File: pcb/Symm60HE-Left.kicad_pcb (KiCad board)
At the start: 2 copper layers, 158.9 x 107.8 mm, 115 parts

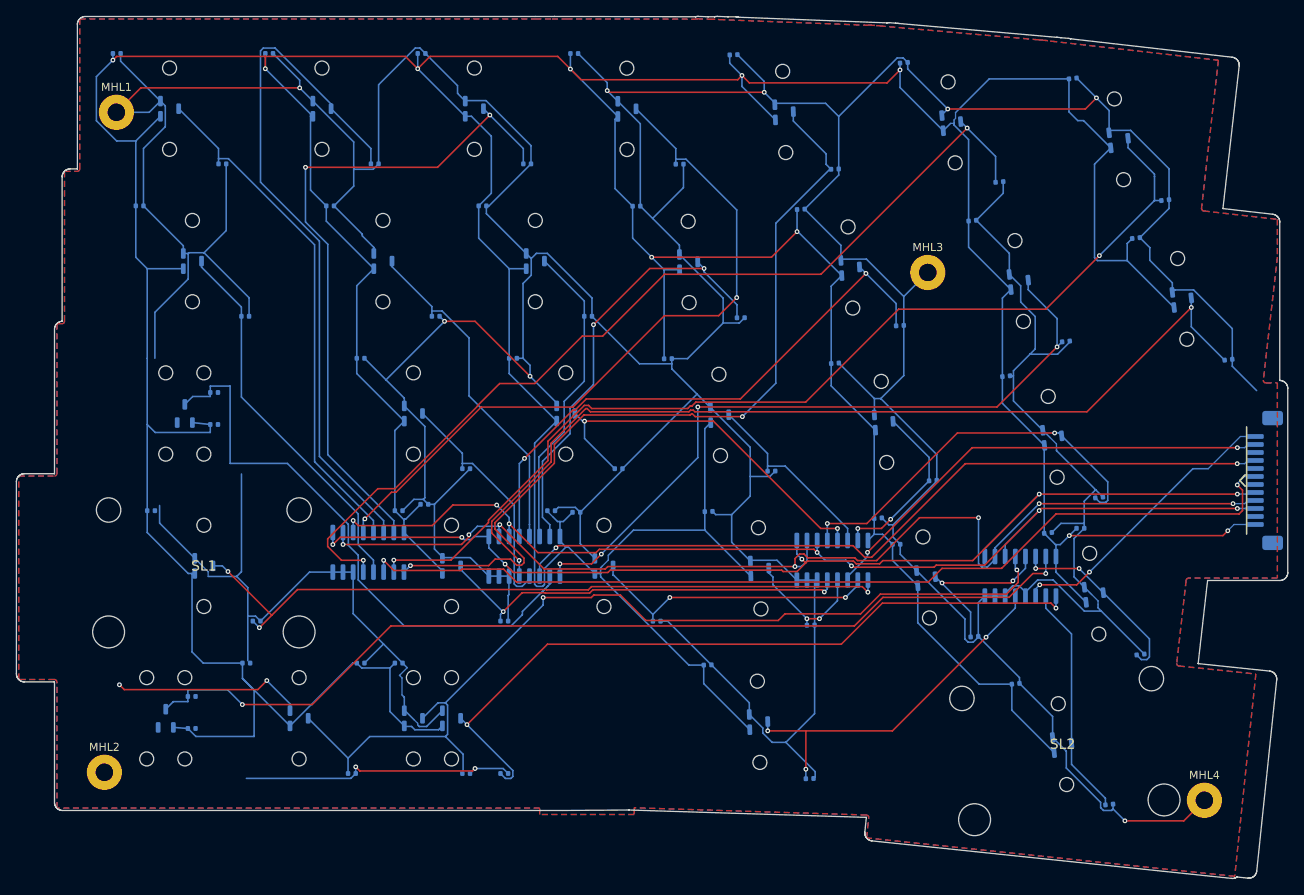
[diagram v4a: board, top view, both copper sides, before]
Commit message: Replace the project with the reorganised T7 tree: ribbon keyboard is production, pogo archived
Production design is now the outward-facing FPC keyboard with per-key
SK6812MINI-E reverse-mount LEDs, a fifth SN74LV4051A mux per half so every
alternate Hall position has its own channel, an SN74AHCT1G125 LED level
shifter, a 50 x 31 mm daughterboard, 1.5 mm POM plates and 3 degree / 7 degree
tent and typing angles. The universal half panel is fully populated (359
placements) with routed NPTH alignment slots for the mutually exclusive
positions, and eight fixed-layout Left/Right PCB pairs are released under
release/layout-pcbs/ with matching BOM, CPL, Gerber ZIP, drill report and DRC.

Reorganise tools/ into cad/, generators/, layouts/, pcb/, pogo/, releases/ and
rendering/ subpackages; add designs/ and layout/ (KLE) trees and per-layout
gallery renders. The Fusion handoff is a fourteen-body reference STEP with
Gateron KS-20 switch and Cherry-profile keycap references and exact BOOMELE,
HRO and XKB models under case/fusion360/models/official/ with provenance.

The Neo-style pogo variant, its Mill-Max vendor models, the Fusion setup
script and the pogo release packages are archived as design history and
marked DO-NOT-ORDER. Their restored BOM snapshots had reintroduced the wrong
mux part C7792; corrected to C128414 / SN74LV4051ADR and their checksum lists
and archives rebuilt.

Co-Authored-By: Claude Opus 5 <noreply@anthropic.com>
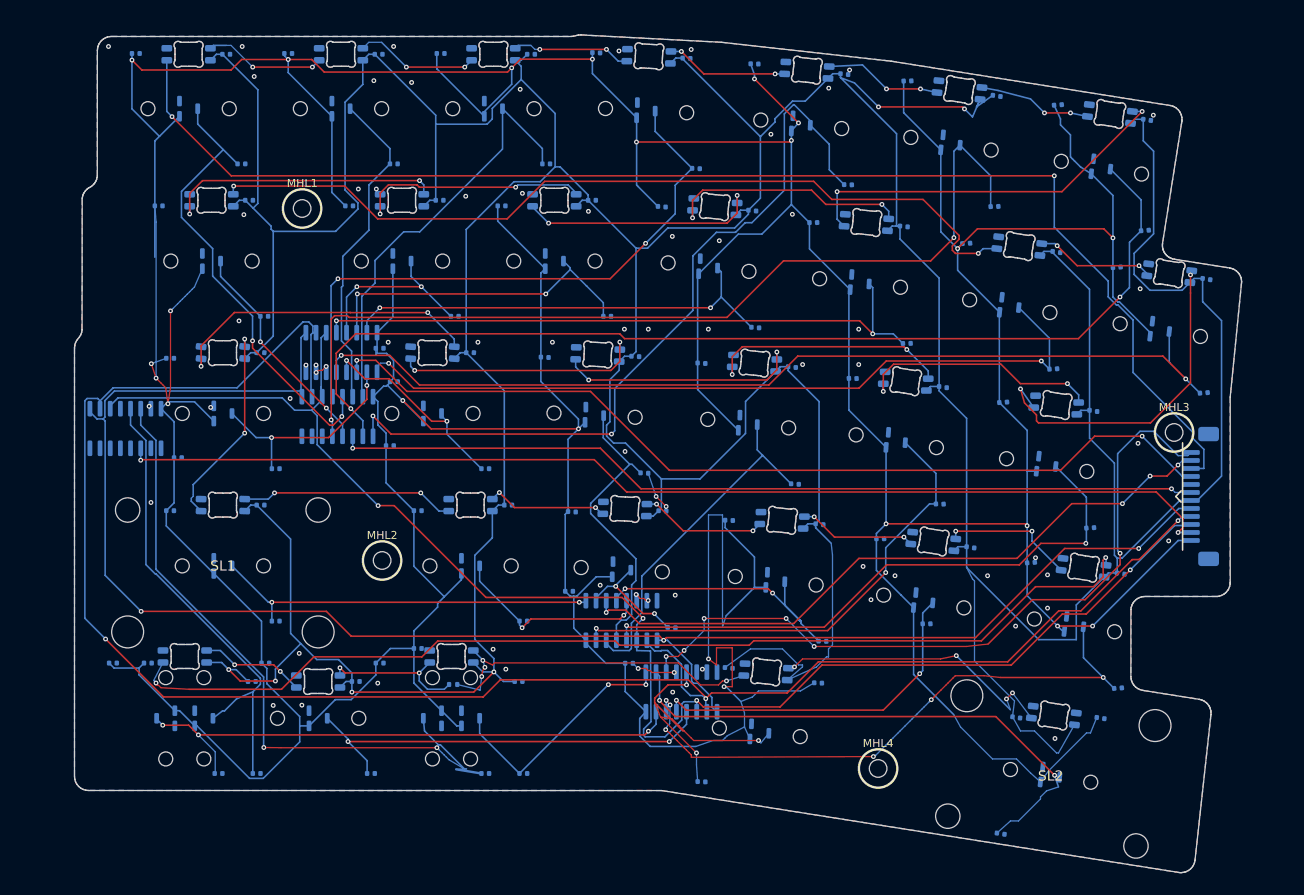
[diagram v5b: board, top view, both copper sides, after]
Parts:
- removed KML15N, KML15S, KML27A, KML27N: MX_MECHANICAL_ONLY, HE_KEY_MECHANICAL_ONLY
- added AML5: SN74LV4051A, Symm60HE_Project:AM1_SOIC-16_3.9x9.9mm_P1.27mm, B.Cu at (5.92, 49.5)
- added CL28A: 100n, Symm60HE_Project:C1_C_0402_1005Metric, B.Cu at (8.71, 78.8)
- added CL28B: 4.7n, Symm60HE_Project:C1_C_0402_1005Metric, B.Cu at (22.3, 92.6)
- added CML5: 100n, Symm60HE_Project:C1_C_0402_1005Metric, B.Cu at (12.5, 53.1)
- added CRGBL1: 100n, Symm60HE_Project:C1_C_0402_1005Metric, B.Cu at (18.5, 2.73)
- added CRGBL10: 100n, Symm60HE_Project:C1_C_0402_1005Metric, B.Cu at (64.2, 21.0)
- added CRGBL11: 100n, Symm60HE_Project:C1_C_0402_1005Metric, B.Cu at (45.2, 21.0)
- added CRGBL12: 100n, Symm60HE_Project:C1_C_0402_1005Metric, B.Cu at (21.4, 21.0)
- added CRGBL13: 100n, Symm60HE_Project:C1_C_0402_1005Metric, B.Cu at (122.3, 27.4)
- added CRGBL14: 100n, Symm60HE_Project:C1_C_0402_1005Metric, B.Cu at (141.0, 30.8)
- added CRGBL15: 100n, Symm60HE_Project:C1_C_0402_1005Metric, B.Cu at (126.9, 47.3)
- added CRGBL16: 100n, Symm60HE_Project:C1_C_0402_1005Metric, B.Cu at (108.1, 44.3)
- added CRGBL17: 100n, Symm60HE_Project:C1_C_0402_1005Metric, B.Cu at (89.2, 41.8)
- added CRGBL18: 100n, Symm60HE_Project:C1_C_0402_1005Metric, B.Cu at (69.6, 40.5)
- added CRGBL19: 100n, Symm60HE_Project:C1_C_0402_1005Metric, B.Cu at (49.0, 40.0)
- added CRGBL2: 100n, Symm60HE_Project:C1_C_0402_1005Metric, B.Cu at (37.6, 2.73)
- added CRGBL20: 100n, Symm60HE_Project:C1_C_0402_1005Metric, B.Cu at (22.8, 40.0)
- added CRGBL21: 100n, Symm60HE_Project:C1_C_0402_1005Metric, B.Cu at (22.8, 59.1)
- added CRGBL22: 100n, Symm60HE_Project:C1_C_0402_1005Metric, B.Cu at (53.8, 59.1)
- added CRGBL23: 100n, Symm60HE_Project:C1_C_0402_1005Metric, B.Cu at (73.0, 59.8)
- added CRGBL24: 100n, Symm60HE_Project:C1_C_0402_1005Metric, B.Cu at (92.7, 61.5)
- added CRGBL25: 100n, Symm60HE_Project:C1_C_0402_1005Metric, B.Cu at (111.5, 64.4)
- added CRGBL26: 100n, Symm60HE_Project:C1_C_0402_1005Metric, B.Cu at (130.3, 67.6)
- added CRGBL27: 100n, Symm60HE_Project:C1_C_0402_1005Metric, B.Cu at (21.7, 81.1)
- added CRGBL29: 100n, Symm60HE_Project:C1_C_0402_1005Metric, B.Cu at (55.1, 81.1)
- added CRGBL3: 100n, Symm60HE_Project:C1_C_0402_1005Metric, B.Cu at (56.6, 2.73)
- added CRGBL30: 100n, Symm60HE_Project:C1_C_0402_1005Metric, B.Cu at (81.3, 79.4)
- added CRGBL31: 100n, Symm60HE_Project:C1_C_0402_1005Metric, B.Cu at (117.3, 85.6)
- added CRGBL33: 100n, Symm60HE_Project:C1_C_0402_1005Metric, B.Cu at (34.7, 81.1)
- added CRGBL4: 100n, Symm60HE_Project:C1_C_0402_1005Metric, B.Cu at (76.0, 3.22)
- added CRGBL5: 100n, Symm60HE_Project:C1_C_0402_1005Metric, B.Cu at (95.8, 5.21)
- added CRGBL6: 100n, Symm60HE_Project:C1_C_0402_1005Metric, B.Cu at (114.8, 7.93)
- added CRGBL7: 100n, Symm60HE_Project:C1_C_0402_1005Metric, B.Cu at (133.6, 10.9)
- added CRGBL8: 100n, Symm60HE_Project:C1_C_0402_1005Metric, B.Cu at (103.2, 24.2)
- added CRGBL9: 100n, Symm60HE_Project:C1_C_0402_1005Metric, B.Cu at (84.3, 22.3)
- added DL1: SK6812MINI-E, Symm60HE_Project:SK6812MINI-E_ReverseMount, B.Cu at (13.8, 2.73)
- added DL10: SK6812MINI-E, Symm60HE_Project:SK6812MINI-E_ReverseMount, B.Cu at (59.5, 21.0)
- added DL11: SK6812MINI-E, Symm60HE_Project:SK6812MINI-E_ReverseMount, B.Cu at (40.5, 21.0)
- added DL12: SK6812MINI-E, Symm60HE_Project:SK6812MINI-E_ReverseMount, B.Cu at (16.7, 21.0)
- added DL13: SK6812MINI-E, Symm60HE_Project:SK6812MINI-E_ReverseMount, B.Cu at (117.6, 26.7)
- added DL14: SK6812MINI-E, Symm60HE_Project:SK6812MINI-E_ReverseMount, B.Cu at (136.4, 30.1)
- added DL15: SK6812MINI-E, Symm60HE_Project:SK6812MINI-E_ReverseMount, B.Cu at (122.3, 46.6)
- added DL16: SK6812MINI-E, Symm60HE_Project:SK6812MINI-E_ReverseMount, B.Cu at (103.5, 43.6)
- added DL17: SK6812MINI-E, Symm60HE_Project:SK6812MINI-E_ReverseMount, B.Cu at (84.6, 41.3)
- added DL18: SK6812MINI-E, Symm60HE_Project:SK6812MINI-E_ReverseMount, B.Cu at (65.0, 40.2)
- added DL19: SK6812MINI-E, Symm60HE_Project:SK6812MINI-E_ReverseMount, B.Cu at (44.3, 40.0)
- added DL2: SK6812MINI-E, Symm60HE_Project:SK6812MINI-E_ReverseMount, B.Cu at (32.9, 2.73)
- added DL20: SK6812MINI-E, Symm60HE_Project:SK6812MINI-E_ReverseMount, B.Cu at (18.1, 40.0)
- added DL21: SK6812MINI-E, Symm60HE_Project:SK6812MINI-E_ReverseMount, B.Cu at (18.1, 59.1)
- added DL22: SK6812MINI-E, Symm60HE_Project:SK6812MINI-E_ReverseMount, B.Cu at (49.1, 59.1)
- added DL23: SK6812MINI-E, Symm60HE_Project:SK6812MINI-E_ReverseMount, B.Cu at (68.3, 59.6)
- added DL24: SK6812MINI-E, Symm60HE_Project:SK6812MINI-E_ReverseMount, B.Cu at (88.0, 61.0)
- added DL25: SK6812MINI-E, Symm60HE_Project:SK6812MINI-E_ReverseMount, B.Cu at (106.9, 63.6)
- added DL26: SK6812MINI-E, Symm60HE_Project:SK6812MINI-E_ReverseMount, B.Cu at (125.7, 66.9)
- added DL27: SK6812MINI-E, Symm60HE_Project:SK6812MINI-E_ReverseMount, B.Cu at (13.3, 78.0)
- added DL29: SK6812MINI-E, Symm60HE_Project:SK6812MINI-E_ReverseMount, B.Cu at (46.7, 78.0)
- added DL3: SK6812MINI-E, Symm60HE_Project:SK6812MINI-E_ReverseMount, B.Cu at (51.9, 2.73)
- added DL30: SK6812MINI-E, Symm60HE_Project:SK6812MINI-E_ReverseMount, B.Cu at (86.0, 79.9)
- added DL31: SK6812MINI-E, Symm60HE_Project:SK6812MINI-E_ReverseMount, B.Cu at (122.0, 85.4)
- added DL33: SK6812MINI-E, Symm60HE_Project:SK6812MINI-E_ReverseMount, B.Cu at (30.0, 81.1)
- added DL4: SK6812MINI-E, Symm60HE_Project:SK6812MINI-E_ReverseMount, B.Cu at (71.4, 2.98)
- added DL5: SK6812MINI-E, Symm60HE_Project:SK6812MINI-E_ReverseMount, B.Cu at (91.1, 4.72)
- added DL6: SK6812MINI-E, Symm60HE_Project:SK6812MINI-E_ReverseMount, B.Cu at (110.2, 7.19)
- added DL7: SK6812MINI-E, Symm60HE_Project:SK6812MINI-E_ReverseMount, B.Cu at (129.0, 10.2)
- added DL8: SK6812MINI-E, Symm60HE_Project:SK6812MINI-E_ReverseMount, B.Cu at (98.5, 23.8)
- added DL9: SK6812MINI-E, Symm60HE_Project:SK6812MINI-E_ReverseMount, B.Cu at (79.6, 21.8)
- added HEL28: MT9102ET, HE_KEY_1.50u, B.Cu at (15.7, 85.7)
- added RBPL29: 0R_DNP, Symm60HE_Project:R3_R_0402_1005Metric, B.Cu at (46.9, 81.5)
- HEL15: footprint HE_SHARED_MIDPOINT -> HE_KEY_1.75u
- HEL27: footprint HE_SHARED_MIDPOINT -> HE_KEY_1.00u
- MHL1, MHL2, MHL3, MHL4: value M2 -> M2_NPTH; footprint Symm60HE_Project:MountingHole_2.2mm_M2_Pad -> Symm60HE_Project:MountingHole_2.2mm_M2_NPTH
- moved CML4 58.9 mm to (68.9, 78.9)
- moved AML4 44.8 mm to (75.4, 82.4), turned to -90 degrees
- moved MHL2 43.7 mm to (38.0, 66.0)
- moved CML3 41.3 mm to (61.4, 69.9)
- moved MHL4 41.0 mm to (100.0, 92.0)
- moved MHL3 36.7 mm to (137.0, 50.0)
- moved AML2 34.2 mm to (32.9, 40.0)
- moved CML2 28.1 mm to (39.5, 43.6)
- moved AML3 27.4 mm to (67.9, 73.5), turned to -90 degrees
- moved MHL1 26.1 mm to (28.0, 22.0)
- moved AML1 17.4 mm to (32.4, 48.0)
- moved CL33B 14.1 mm to (115.3, 100.2), turned to -9 degrees
- moved CL32A 14.0 mm to (92.5, 81.3), turned to -2.444 degrees
- moved CL32B 13.5 mm to (77.9, 93.7), turned to -2.444 degrees
- moved CL27A 12.8 mm to (4.35, 78.8)
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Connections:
- CL30B pad 1: HE_L28 -> HE_L33
- HEL30 pad 3: HE_L28 -> HE_L33
- JL1 pad 11: GND -> ADC_L5
- JL1 pad 3: GND -> RGB_L
- JL1 pad 7: GND -> VBUS
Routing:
- net GND: track 1037.8 -> 16.4 mm, vias 12 -> 69
- net VBUS: track 0.00 -> 770.8 mm, vias 0 -> 6
- net RGB_L: track 0.00 -> 166.7 mm, vias 0 -> 2
- net ADC_L5: track 0.00 -> 138.4 mm, vias 0 -> 2
- net RGB_L_26: track 0.00 -> 131.6 mm, vias 0 -> 2
- net RGB_L_12: track 0.00 -> 106.3 mm, vias 0 -> 2
- net MUX_A1: track 137.9 -> 238.3 mm, vias 7 -> 3
- net +3V3A: track 845.1 -> 942.3 mm, vias 10 -> 22
- net HE_L33: track 0.00 -> 88.1 mm, vias 0 -> 2
- net MUX_A2: track 137.7 -> 216.8 mm, vias 6 -> 3
- net HE_L28: track 120.3 -> 53.8 mm
- net HE_L29: track 93.6 -> 30.9 mm
- net MUX_A0: track 132.3 -> 192.4 mm, vias 7 -> 4
- net HE_L32: track 0.00 -> 58.9 mm
- net ADC_L4: track 35.3 -> 93.0 mm, vias 2 -> 6
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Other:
- board size 158.9 x 107.8 mm -> 145.9 x 104.7 mm

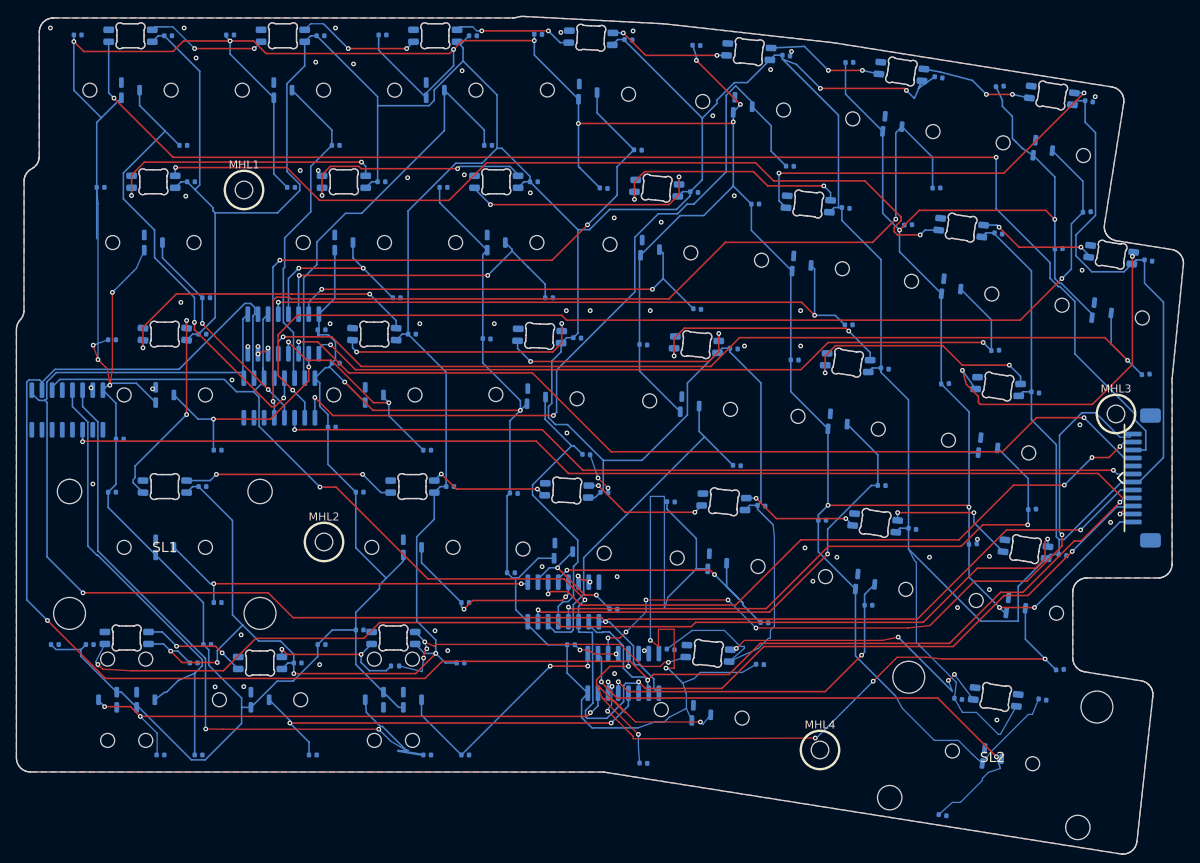
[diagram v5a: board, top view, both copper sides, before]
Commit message: Move every LED into the switch's south RGB pocket
The reverse-mount SK6812MINI-E sat 7.60 mm north of each key, shining into
the Gateron KS-20's opaque cover rather than its window. All 65 LEDs now sit
5.35 mm south of their key, in the pocket the cover is moulded for, so the
board lights like a Wooting 60HE+ backlight instead of a pass-through for a
transparent cap. Switches install with their RGB pocket toward the user; the
plate cutout and the alignment pins are symmetric, so nothing else changes.

Both halves were re-routed around the new apertures and are fully connected
with no DRC errors: 247 vias on the left (was 251) and 418 on the right (was
393). A handful of GND pads the apertures fence off on both layers reach the
plane through a via inside the pad, so the order checklist now asks for tented
vias. The pours' copies of the apertures moved with the LEDs -- they had been
left behind at the old positions, cutting some 800 mm2 of ground per layer for
openings that were no longer there.

The fixed-layout derivatives needed more than a copy of that work. Each one
restores its close-pair switches' alignment drills to the horizontal axis, and
the masters' new routing ran where those drills land, so the finishing pass
grew a repair loop: give a finding room, route it again, and keep the result
only if nothing got worse -- no new opens, and never a short. A net the router
cannot put back keeps the copper it had. Where a gap is short by microns the
trace is bent clear rather than ripped, because on a board this full a ripped
trace comes back exactly where it was. An LED only returns to its fixed-layout
row when that space is free, and the stabilisers keep the master's angle now
that they no longer have a northern aperture to face. All sixteen boards report
zero DRC and connectivity errors, and the audit checks the pocket window rather
than a nominal offset.

The panel gained the same care: a break row would have drilled through a trace
running along the right half'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
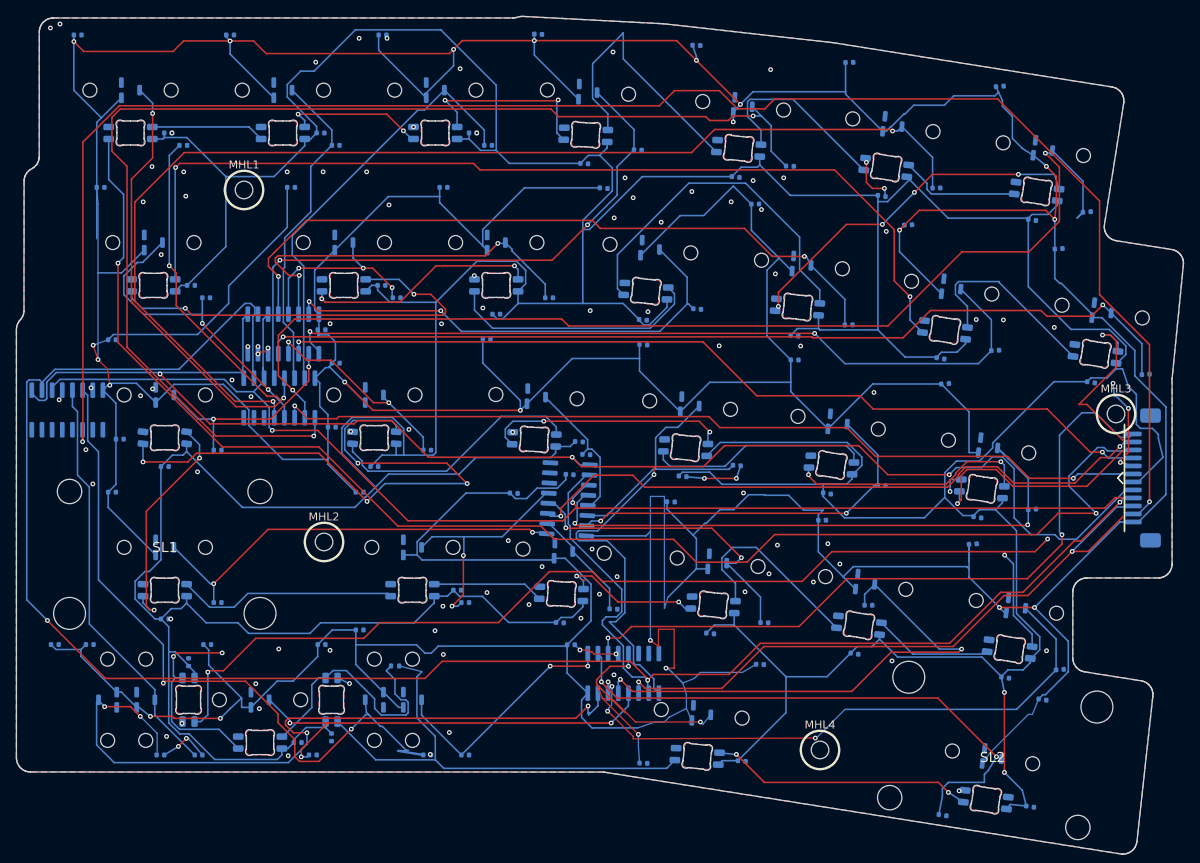
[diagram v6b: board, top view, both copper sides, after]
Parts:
- moved CRGBL29 18.6 mm to (38.9, 90.4), turned to -90 degrees
- moved CRGBL17 17.2 mm to (82.8, 57.8)
- moved CRGBL19 17.2 mm to (44.3, 56.6)
- moved CRGBL20 17.2 mm to (18.1, 56.6)
- moved CRGBL21 17.2 mm to (18.1, 75.6)
- moved CRGBL8 17.2 mm to (96.8, 40.2)
- moved CRGBL13 17.2 mm to (115.1, 43.1)
- moved CRGBL10 17.2 mm to (59.5, 37.5)
- moved CRGBL25 17.2 mm to (104.3, 80.0)
- moved CRGBL9 17.2 mm to (77.9, 38.2)
- moved CRGBL24 17.2 mm to (86.3, 77.4)
- moved CRGBL15 17.2 mm to (119.7, 62.9)
- moved CRGBL16 17.2 mm to (100.9, 59.9)
- moved CRGBL23 17.2 mm to (67.5, 76.1)
- moved CRGBL26 16.9 mm to (123.1, 83.0)
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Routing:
- net +3V3A: track 942.3 -> 1059.3 mm, vias 22 -> 21
- net ADC_L5: track 138.4 -> 218.5 mm
- net HE_L05: track 98.5 -> 152.0 mm
- net MUX_A0: track 192.4 -> 244.1 mm
- net HE_L01: track 57.7 -> 94.6 mm, vias 2 -> 3
- net RGB_L_19: track 39.2 -> 74.3 mm, vias 2 -> 4
- net GND: track 16.4 -> 47.2 mm, vias 69 -> 104
- net VBUS: track 770.8 -> 801.5 mm, vias 6 -> 2
- net HE_L06: track 118.1 -> 146.2 mm
- net MUX_A1: track 238.3 -> 260.8 mm
- net HE_L27: track 72.0 -> 94.0 mm, vias 3 -> 4
- net HE_L25: track 43.8 -> 64.7 mm
- net RGB_L_04: track 15.4 -> 34.2 mm, vias 2 -> 0
- net HE_L17: track 37.0 -> 18.5 mm
- net RGB_L_11: track 34.9 -> 53.1 mm
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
